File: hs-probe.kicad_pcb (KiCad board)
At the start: 4 copper layers, 40 x 14 mm, 55 parts, among them J1 USB_C_Receptacle_USB2.0, J2 Castellated Vias, J3 Castellated Vias, J4 Castellated Vias, J5 tag-connect-swd, U1 hs-probe-stm32, U2 12 MHz, U3 MIC5353, U4 NUF8401MNT4G, U5 STDC14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

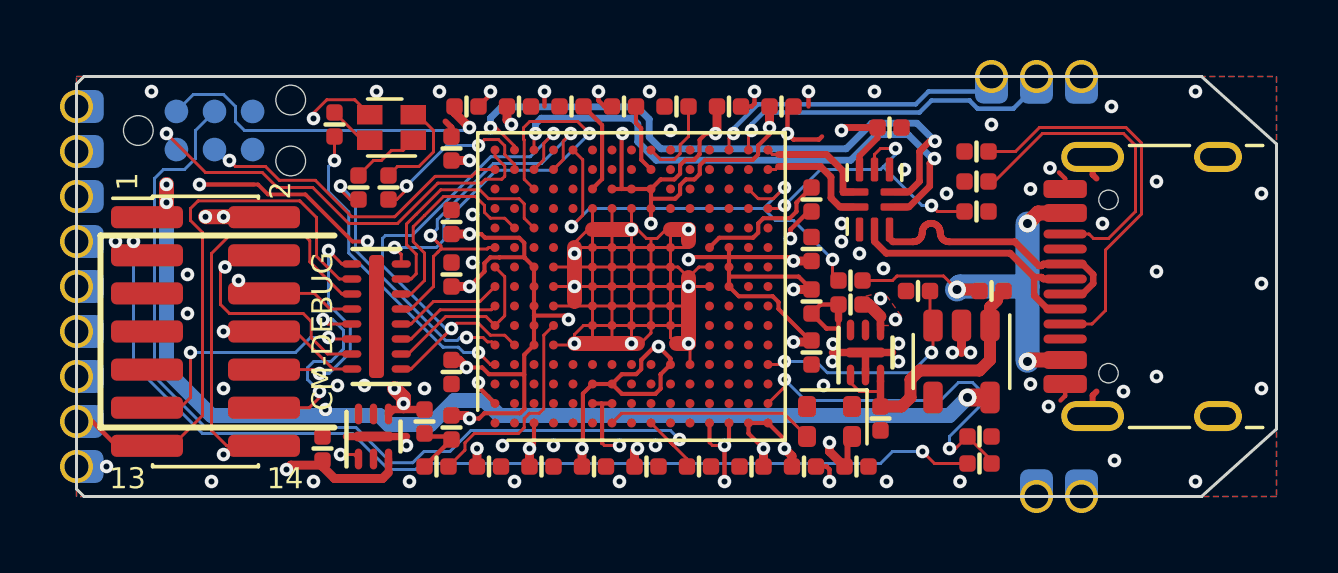
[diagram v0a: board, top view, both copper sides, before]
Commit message: Added 5V target sense line
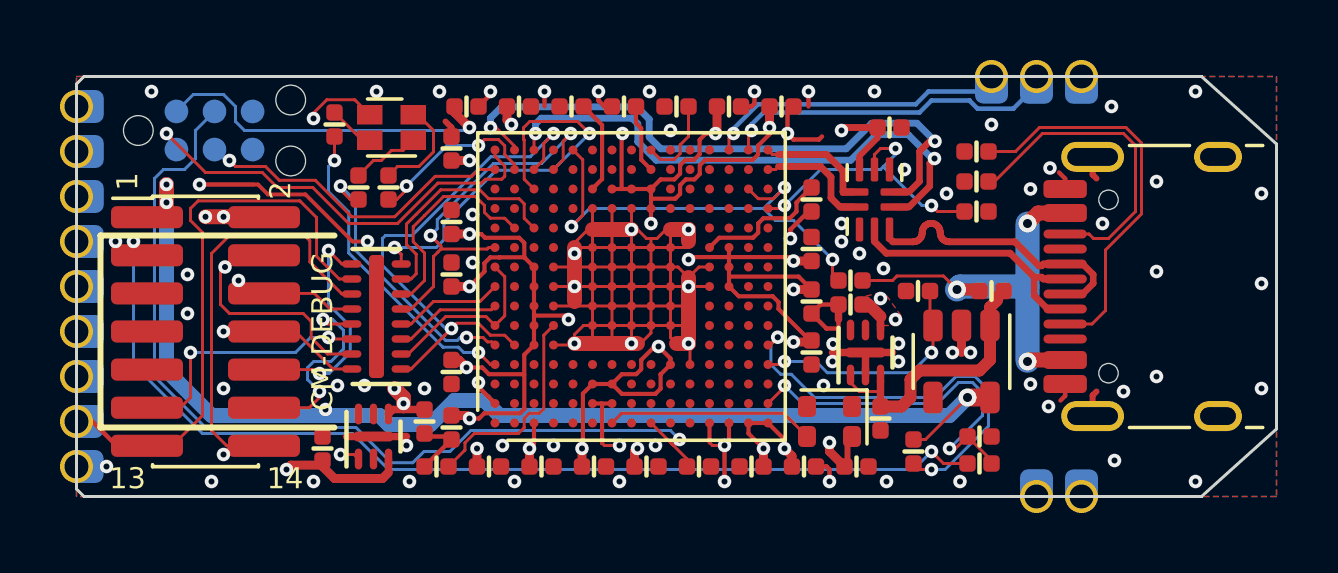
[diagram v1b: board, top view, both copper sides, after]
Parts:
- added R103: 5.1k, passive:R_0402, F.Cu at (176.4, 91.5)
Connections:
- U1 pad R5: Net-(U1-PadR5) -> /PROT_5V_SENSE
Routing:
- net /PROT_5V_SENSE: track 0.00 -> 14.0 mm, vias 0 -> 2
- net /PROTECTED_5V: track 49.8 -> 52.2 mm

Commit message: v1.3, now can connect 5V to pin 7 of STDC14
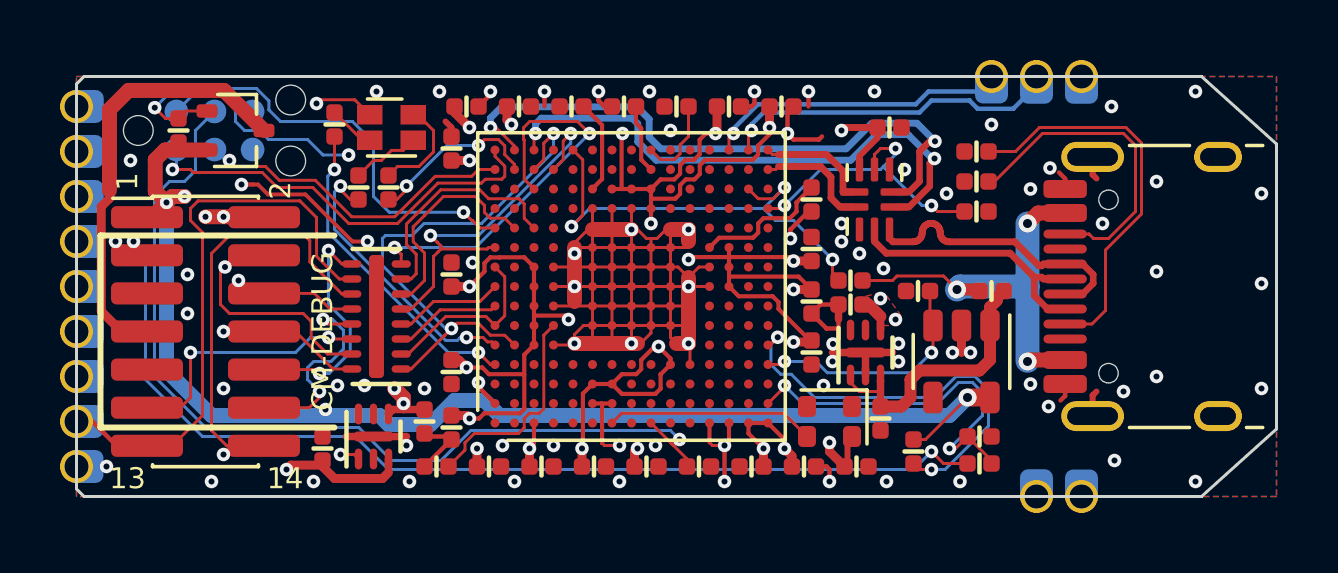
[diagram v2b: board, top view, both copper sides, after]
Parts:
- removed C10: 0.1u, passive:C_0402
- added Q101: DMP2110UW-7, sot:SOT-323, F.Cu at (153.8, 80.8)
- added R104: 5.1k, passive:R_0402, F.Cu at (151.9, 80.8)
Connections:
- U1 pad A11: Net-(U1-PadA11) -> /5V_KEY_EN
- U5 pad 7: GND -> /5V_KEY
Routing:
- net /5V_KEY_EN: track 0.00 -> 16.8 mm, vias 0 -> 2
- net /5V_KEY: track 0.00 -> 14.6 mm
- net +3V3: track 86.0 -> 82.3 mm
- net /PROTECTED_5V: track 52.2 -> 55.0 mm
- net GND: track 97.0 -> 95.6 mm, vias 77 -> 76
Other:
- board text added: "HS Probe v1.3 By Emil Fresk @korken89"
- board text added: "VCP RX"
- board text added: "VCP TX"
- board text removed: "HS Probe v1.2 By Emil Fresk @korken89"
- board text removed: "RX"
- board text removed: "TX"

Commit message: Changed ferrite bead for fuse
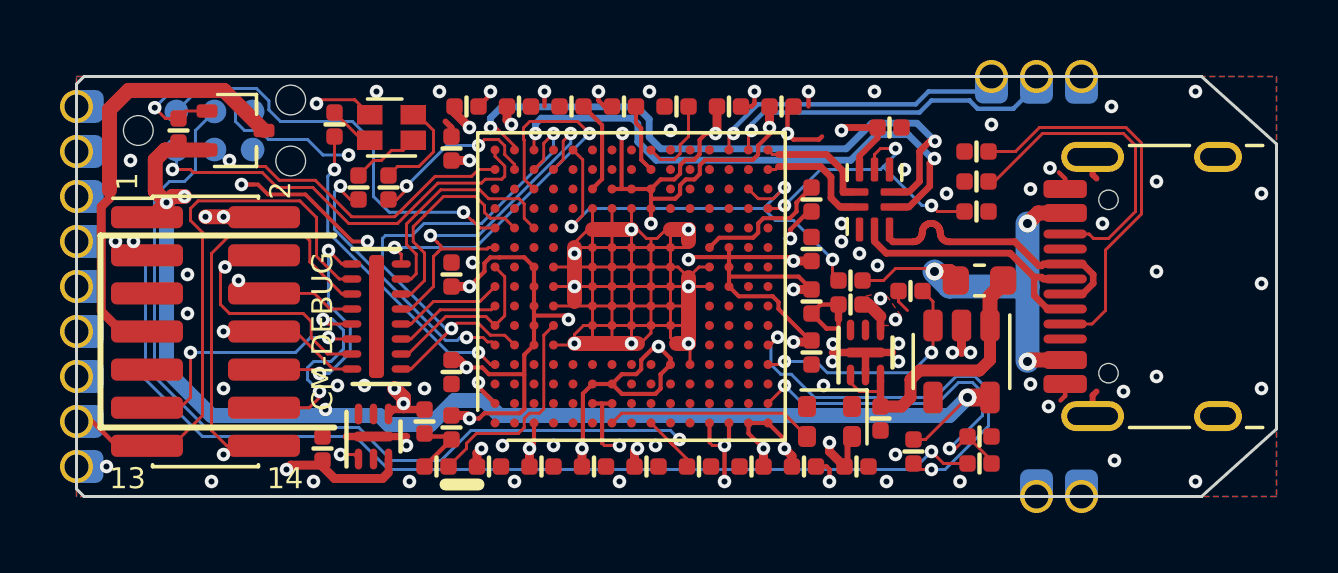
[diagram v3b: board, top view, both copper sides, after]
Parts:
- removed FB1: Ferrite_Bead_Small, passive:R_0402
- added F101: Fuse_Small, Fuse:Fuse_0603_1608Metric, F.Cu at (178.6, 85.8)
- moved R10 0.25 mm to (176.3, 86.2)
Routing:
- net GND: track 95.6 -> 96.4 mm, vias 76 -> 77

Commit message: v1.4, now without the USB mux
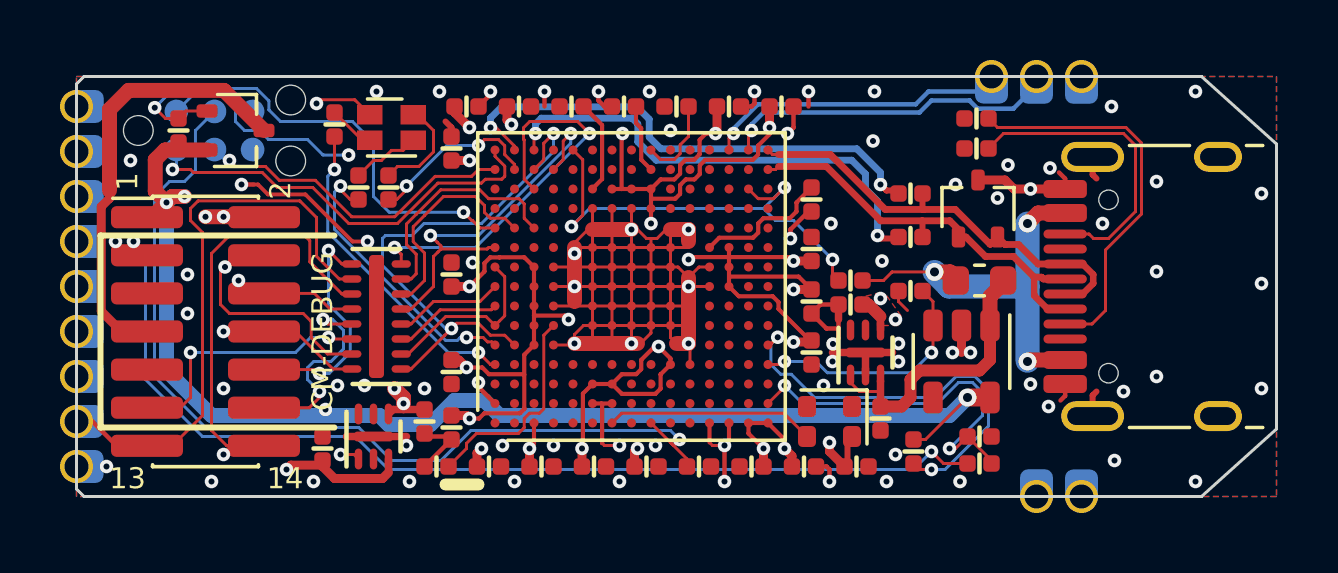
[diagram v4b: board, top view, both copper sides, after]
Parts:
- removed C28: 0.1u, passive:C_0402
- removed U8: USB3740B-AI9, Package_DFN_QFN:UQFN-10_1.6x2.1mm_P0.5mm
- added D2: ESD7002WTT1G, sot:SOT-323, F.Cu at (178.6, 83.4)
- added R11: 39, passive:R_0402, F.Cu at (176.3, 84.3)
- R8: value 5.1k -> 39
- U6: value MAX40203AUK -> MAX40203AUK or MAX40200AUK
- moved R8 2.28 mm to (176.3, 82.9), turned to 180 degrees
- moved R3 1.10 mm to (178.5, 80.4)
- moved R4 1.10 mm to (178.5, 81.4)
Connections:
- J1 pad A6: /D_P -> /D_HS_P
- J1 pad A7: /D_N -> /D_HS_N
- J1 pad B6: /D_P -> /D_HS_P
- J1 pad B7: /D_N -> /D_HS_N
- R8 pad 1: /USB_SEL -> /D_HS_P
- R8 pad 2: GND -> /D_FS_P
- U1 pad R12: /USB_SEL -> Net-(U1-PadR12)
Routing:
- net /D_HS_P: track 3.86 -> 14.8 mm
- net /D_HS_N: track 3.89 -> 14.1 mm
- net /USB_SEL: track 9.81 -> 0.00 mm, vias 3 -> 0
- net /D_P: track 9.73 -> 0.00 mm
- net /D_N: track 9.10 -> 0.00 mm
- net /D_FS_P: track 20.6 -> 17.0 mm
- net +3V3: track 82.4 -> 79.5 mm, vias 27 -> 26
- net /D_FS_N: track 18.3 -> 16.0 mm
- net GND: track 96.4 -> 98.1 mm, vias 77 -> 76
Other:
- board text added: "HS Probe v1.4 By Emil Fresk @korken89"
- board text removed: "HS Probe v1.3 By Emil Fresk @korken89"

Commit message: v2.0 and kicad v6
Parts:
- removed C22, C23: 0.1u, passive:C_0402
- added C101: 2.2u, passive:C_0402, F.Cu at (174.9, 80.1)
- added R105: 100k, passive:R_0402, F.Cu at (160.1, 90.1)
- added R106: 135k, passive:R_0402, F.Cu at (156.9, 89.7)
- added R107: 90k, passive:R_0402, F.Cu at (158.5, 89.2)
- added R108: 100k, passive:R_0402, F.Cu at (174.9, 86.4)
- added R109: 135k, passive:R_0402, F.Cu at (174.9, 84.6)
- added R110: 90k, passive:R_0402, F.Cu at (174.9, 85.5)
- added U101: MIC5504, dfn:UDFN-4_1x1mm_P0.65mm, F.Cu at (176.7, 80.7)
- moved C25 2.27 mm to (176.0, 88.1), turned to -90 degrees
- moved R8 2.20 mm to (174.9, 81.2)
- moved R11 2.20 mm to (174.9, 82.7)
- moved R9 2.18 mm to (174.9, 83.7)
- moved R1 1.70 mm to (162.2, 92.0)
- moved C27 1.55 mm to (160.5, 92.0), turned to 0 degrees
- moved R10 0.66 mm to (176.4, 85.5), turned to 90 degrees
- moved U4 0.50 mm to (158.5, 86.5)
- moved U3 0.30 mm to (174.5, 88.2)
- moved U6 0.30 mm to (178.3, 88.5)
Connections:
- net /T_~RESET renamed /T_~{RESET}
- net Net-(C24-Pad1) renamed /FUSED_5V
- C18 pad 1: +3V3 -> +1V8
- U1 pad N4: Net-(U1-PadN4) -> /VS_MAIN
- U1 pad P1: +3V3 -> +1V8
- U1 pad P4: Net-(U1-PadP4) -> /VS_T
- U3 pad 5: (no net) -> /ADJ_MAIN
- U5 pad 7: /5V_KEY -> GND
- U5 pad 9: Net-(U5-Pad9) -> /5V_KEY
- U7 pad 5: (no net) -> /ADJ_T
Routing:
- net +1V8: track 0.00 -> 20.9 mm, vias 0 -> 2
- net /VS_T: track 0.00 -> 18.5 mm, vias 0 -> 2
- net /VS_MAIN: track 0.00 -> 7.14 mm
- net /FUSED_5V: track 9.74 -> 16.7 mm, vias 0 -> 2
- net +3V3: track 79.5 -> 73.1 mm, vias 26 -> 23
- net /ADJ_T: track 0.00 -> 4.12 mm
- net GND: track 98.1 -> 101.9 mm, vias 76 -> 70
- net /ADJ_MAIN: track 0.00 -> 3.51 mm
- net /T_VCC: track 83.5 -> 86.9 mm
- net /D_FS_N: track 16.0 -> 13.0 mm
- net /D_FS_P: track 17.0 -> 15.1 mm
- net /BOOT0: track 7.16 -> 5.64 mm
- net /5V_KEY: track 14.6 -> 15.9 mm
- net +5V: track 63.2 -> 64.2 mm
- net /T_VCC_EN: track 7.18 -> 7.97 mm
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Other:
- net class Default removed
- rule pad_to_mask_clearance: 0.05 -> 0
- board text added: "CM-DBG"
- board text added: "HS Probe v2.0 By Emil Fresk @korken89"
- board text removed: "CM-DEBUG"
- board text removed: "HS Probe v1.4 By Emil Fresk @korken89"
